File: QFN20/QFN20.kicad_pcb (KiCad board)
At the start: 2 copper layers, 25.4 x 12.7 mm, 9 parts, among them J1 Conn_01x10, J2 Conn_02x10_Counter_Clockwise, J3 Conn_01x10, J4 Conn_02x10_Counter_Clockwise, J5 Conn_01x03

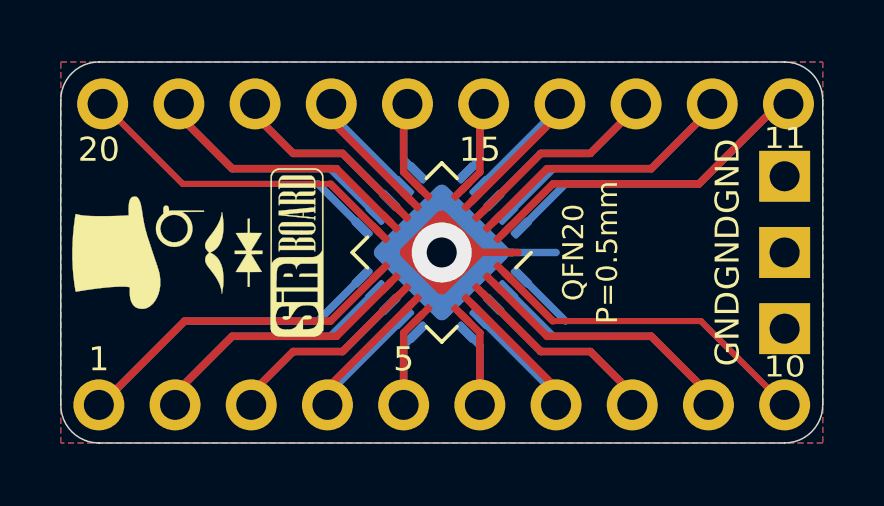
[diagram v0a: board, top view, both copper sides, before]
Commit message: Breakout Boards Revision 2
Renders updated, silkscreen text improved, blurry silkscreen items removed/resized.
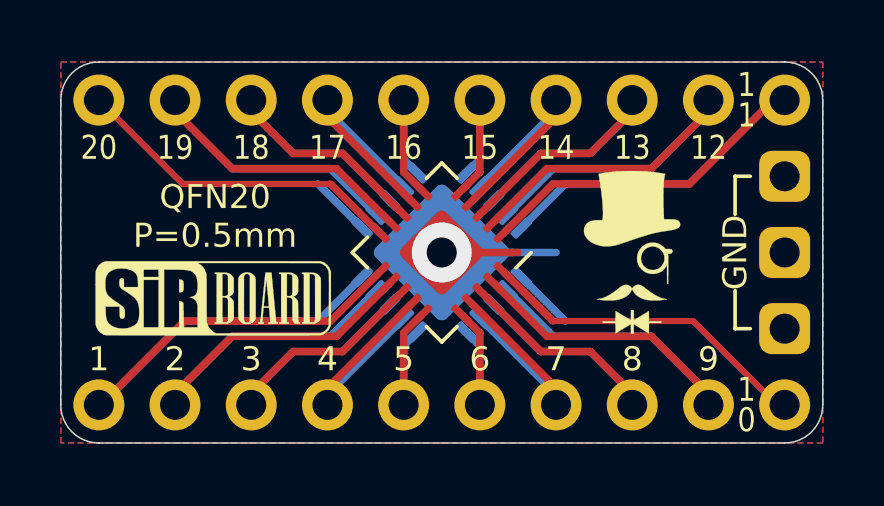
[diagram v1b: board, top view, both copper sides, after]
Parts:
- removed the G*** at (61.1, 42.0)
- removed the G*** at (65.5, 42.2)
- added G***: LOGO, logo:SirBoard79x25, B.Cu at (62.7, 43.7)
- added G***: LOGO, logo:logo54x76, B.Cu at (76.7, 42.2)
- G***: footprint logo:SirBoard56x18 -> logo:SirBoard79x25
- G***: footprint logo:logo63x89 -> logo:logo54x76
- moved G*** 15.5 mm to (76.7, 42.2), turned to 0 degrees
- moved G*** 3.18 mm to (62.7, 43.7), turned to 0 degrees
- moved J1 0.18 mm to (81.8, 37.1)
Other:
- board text added: "0"
- board text added: "12"
- board text added: "13"
- board text added: "14"
- board text added: "16"
- board text added: "17"
- board text added: "18"
- board text added: "19"
- board text added: "2"
- board text added: "3"
- board text added: "4"
- board text added: "6"
- board text added: "7"
- board text added: "8"
- board text added: "9"
- board text removed: "10"
- board text removed: "11"
